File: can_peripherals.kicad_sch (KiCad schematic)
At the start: 24 parts, among them U2 MCP2551, U5 MCP2515, Y1 ABLS7M-16.000MHZ-B-2-T

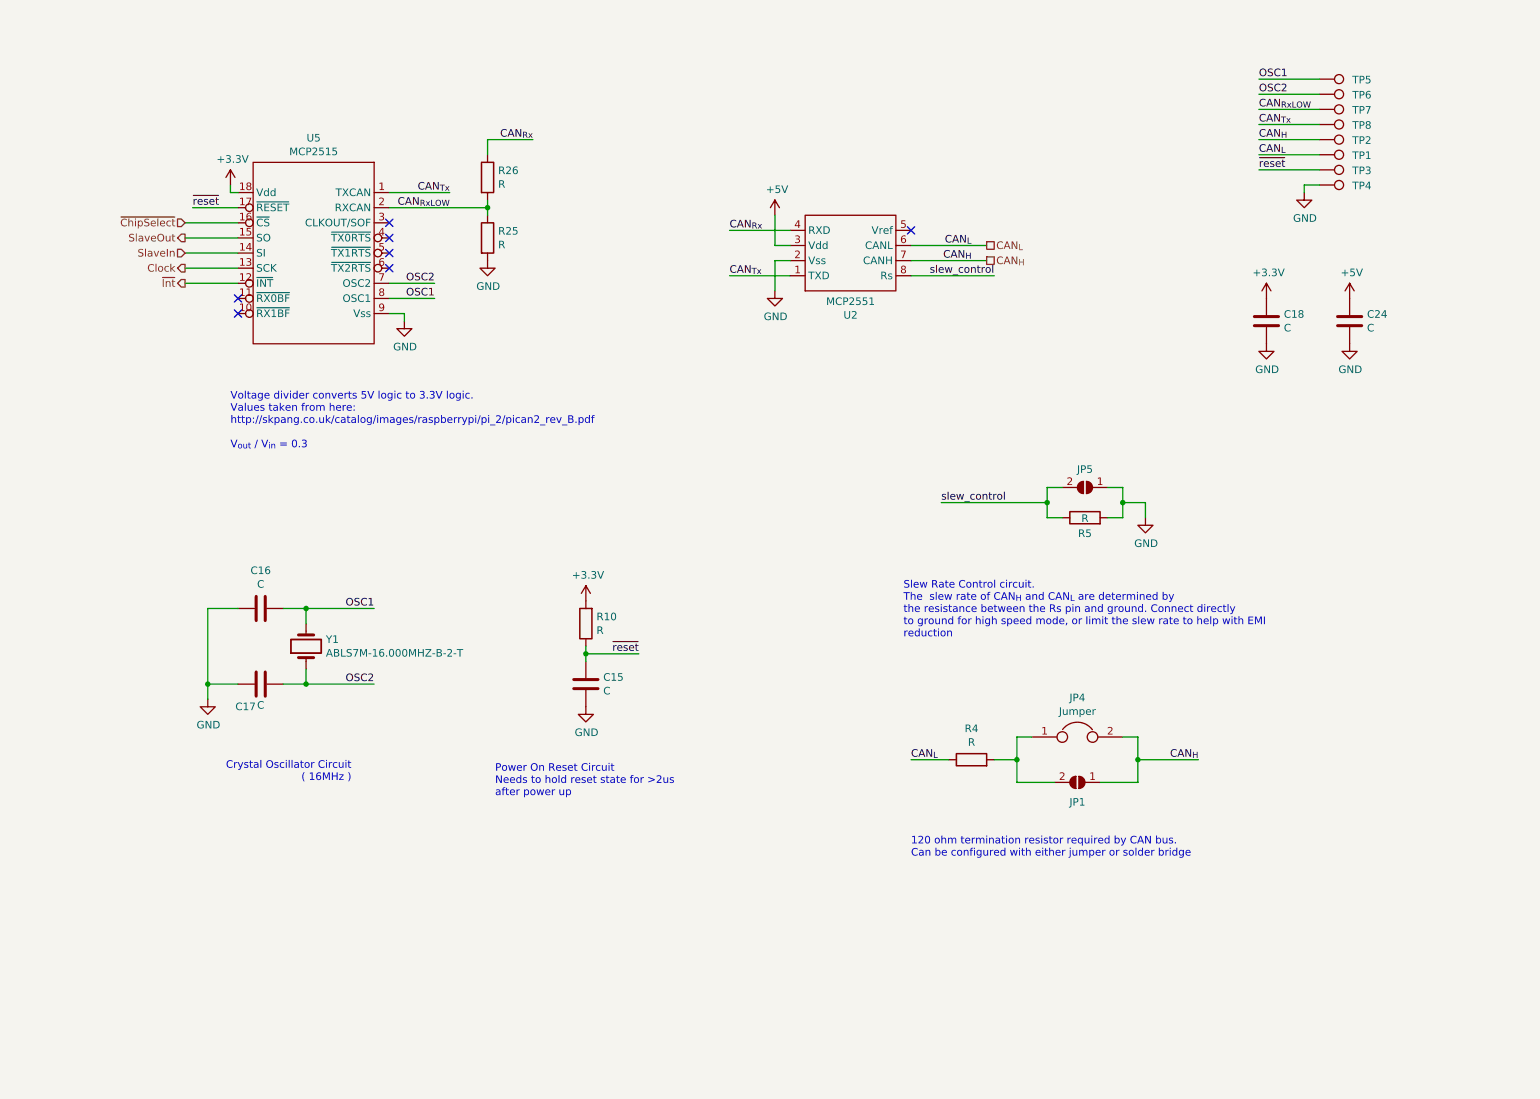
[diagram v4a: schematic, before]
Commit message: tweaked CAN interface
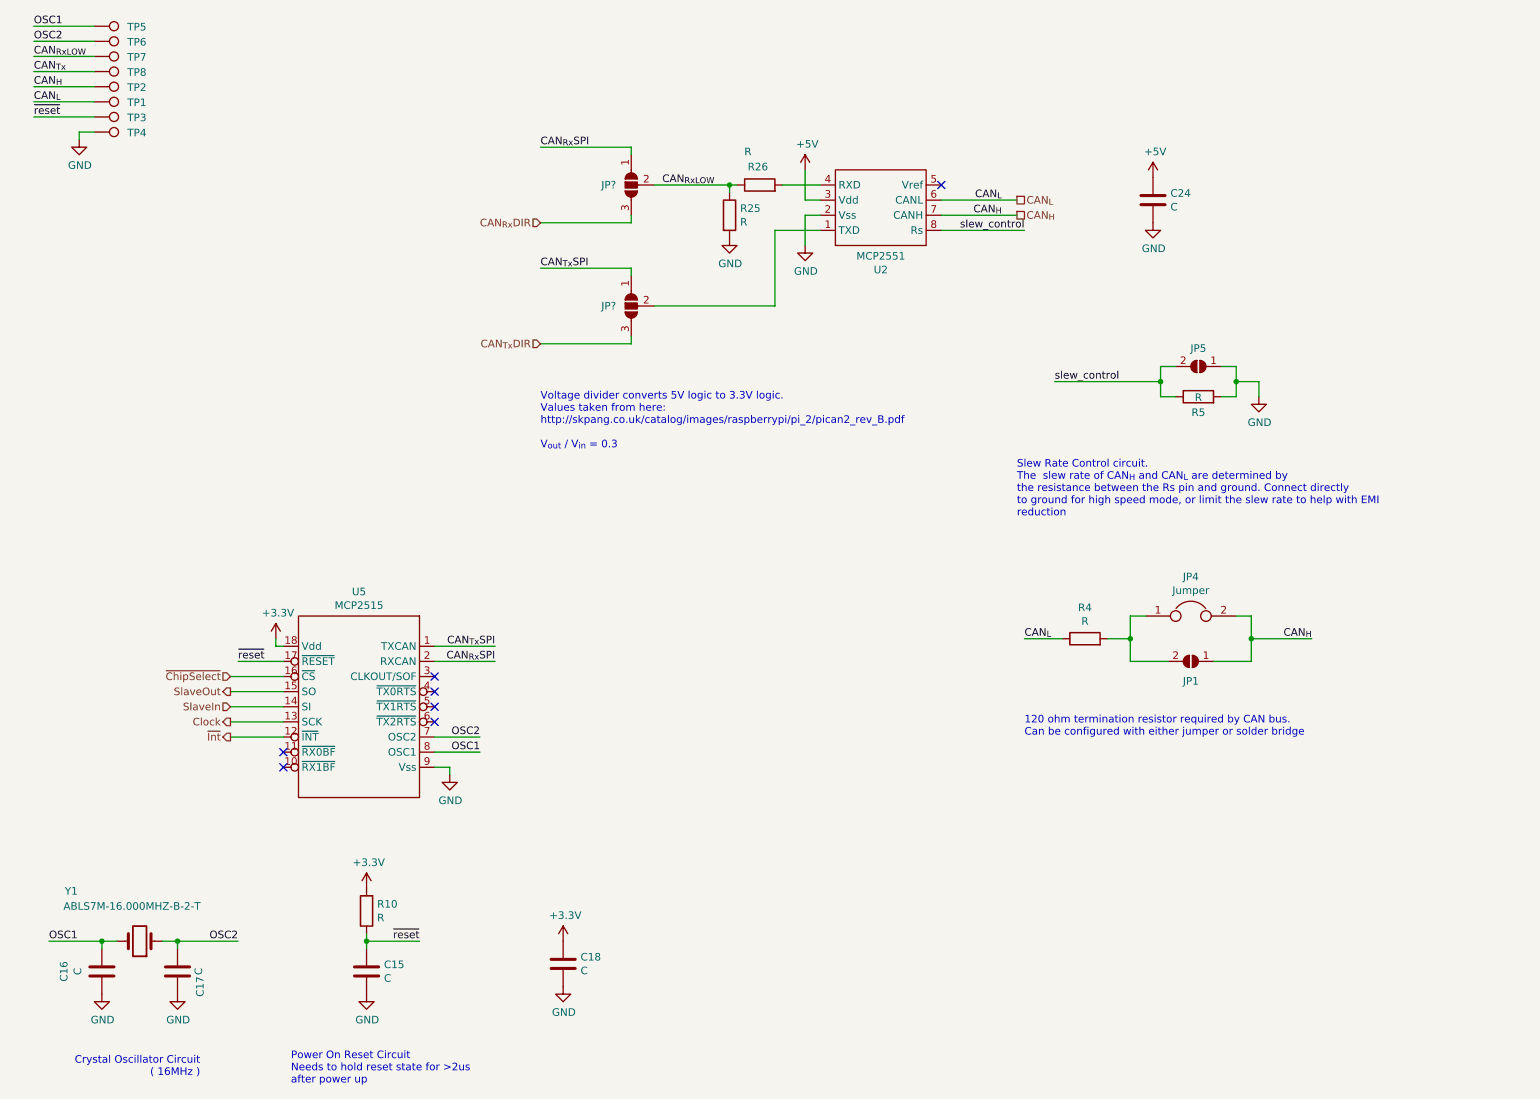
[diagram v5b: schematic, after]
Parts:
- added JP? (x2): SolderJumper_3_Open, symbol Jumper:SolderJumper_3_Open
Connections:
- net CAN_{RxLOW}: now also R26.1, JP?.2 (C); no longer R26.2, U5.2 (RXCAN)
- net CAN_{Tx}: no longer U2.1 (TXD), U5.1 (TXCAN)
- net CAN_{Rx}: no longer names the net of U2.4 (RXD)
- net CAN_{Rx}: now also R26.2; no longer R26.1
- new net: JP?.2 (C), U2.1 (TXD)
- new net CAN_{Rx}DIR: JP?.3 (B)
- new net CAN_{Rx}SPI: JP?.1 (A), U5.2 (RXCAN)
- new net CAN_{Tx}DIR: JP?.3 (B)
- new net CAN_{Tx}SPI: JP?.1 (A), U5.1 (TXCAN)
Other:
- moved on the sheet: C15, C16, C17, C18, C24, JP1, JP4, JP5, R10, R25, R26, R4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

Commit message: layout sketching
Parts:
- JP7, JP8: renamed from JP?; footprint (none) -> Jumper:SolderJumper-3_P1.3mm_Open_RoundedPad1.0x1.5mm_NumberLabels
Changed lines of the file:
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@@
   (symbol (lib_id "power:GND") (at 29.21 184.15 0) (unit 1)
     (in_bom yes) (on_board yes)
-    (property "Reference" "#PWR?" (id 0) (at 29.21 190.5 0)
+    (property "Reference" "#PWR0101" (id 0) (at 29.21 190.5 0)
       (effects (font (size 1.27 1.27)) hide)
     )
@@
   (symbol (lib_id "power:GND") (at 41.91 184.15 0) (unit 1)
     (in_bom yes) (on_board yes)
-    (property "Reference" "#PWR?" (id 0) (at 41.91 190.5 0)
+    (property "Reference" "#PWR0104" (id 0) (at 41.91 190.5 0)
       (effects (font (size 1.27 1.27)) hide)
     )
@@
   (symbol (lib_id "Jumper:SolderJumper_3_Open") (at 118.11 48.26 90) (mirror x) (unit 1)
     (in_bom yes) (on_board yes) (fields_autoplaced)
-    (property "Reference" "JP?" (id 0) (at 115.57 48.2599 90)
+    (property "Reference" "JP7" (id 0) (at 115.57 48.2599 90)
       (effects (font (size 1.27 1.27)) (justify left))
     )
@@
       (effects (font (size 1.27 1.27)) (justify left) hide)
     )
-    (property "Footprint" "" (id 2) (at 118.11 48.26 0)
+    (property "Footprint" "Jumper:SolderJumper-3_P1.3mm_Open_RoundedPad1.0x1.5mm_NumberLabels" (id 2) (at 118.11 48.26 0)
       (effects (font (size 1.27 1.27)) hide)
     )
@@
   (symbol (lib_id "Jumper:SolderJumper_3_Open") (at 118.11 68.58 90) (mirror x) (unit 1)
     (in_bom yes) (on_board yes) (fields_autoplaced)
-    (property "Reference" "JP?" (id 0) (at 115.57 68.5799 90)
+    (property "Reference" "JP8" (id 0) (at 115.57 68.5799 90)
       (effects (font (size 1.27 1.27)) (justify left))
     )
@@
       (effects (font (size 1.27 1.27)) (justify left) hide)
     )
-    (property "Footprint" "" (id 2) (at 118.11 68.58 0)
-      (effects (font (size 1.27 1.27)) hide)
-    )
+    (property "Footprint" "Jumper:SolderJumper-3_P1.3mm_Open_RoundedPad1.0x1.5mm_NumberLabels" (id 2) (at 118.11 68.58 0)
+      (effects (font (size 1.27 1.27)) hide)
+    )

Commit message: WIP
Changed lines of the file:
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@@
     (effects (font (size 1.27 1.27)) (justify right))
   )
-  (hierarchical_label "CAN_{Rx}DIR" (shape input) (at 102.87 54.61 180)
+  (hierarchical_label "CAN_{Rx}DIR" (shape output) (at 102.87 54.61 180)
     (effects (font (size 1.27 1.27)) (justify right))
   )

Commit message: finished routing
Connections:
- net CAN_{Tx}: now also JP8.2 (C), U2.1 (TXD)
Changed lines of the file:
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@@
+    (effects (font (size 1.27 1.27)) (justify left bottom))
+  )
+  (label "CAN_{Tx}" (at 123.19 68.58 0)
     (effects (font (size 1.27 1.27)) (justify left bottom))
   )
